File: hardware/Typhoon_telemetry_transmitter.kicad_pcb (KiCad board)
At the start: 2 copper layers, 36.5 x 26 mm, 20 parts, among them J1 Conn_01x04_Pin, J3 Conn_ST_STDC14, SW1 SW_Push, U1 STM32F103C8Tx, U2 NRF24L01_Breakout, Y1 8M

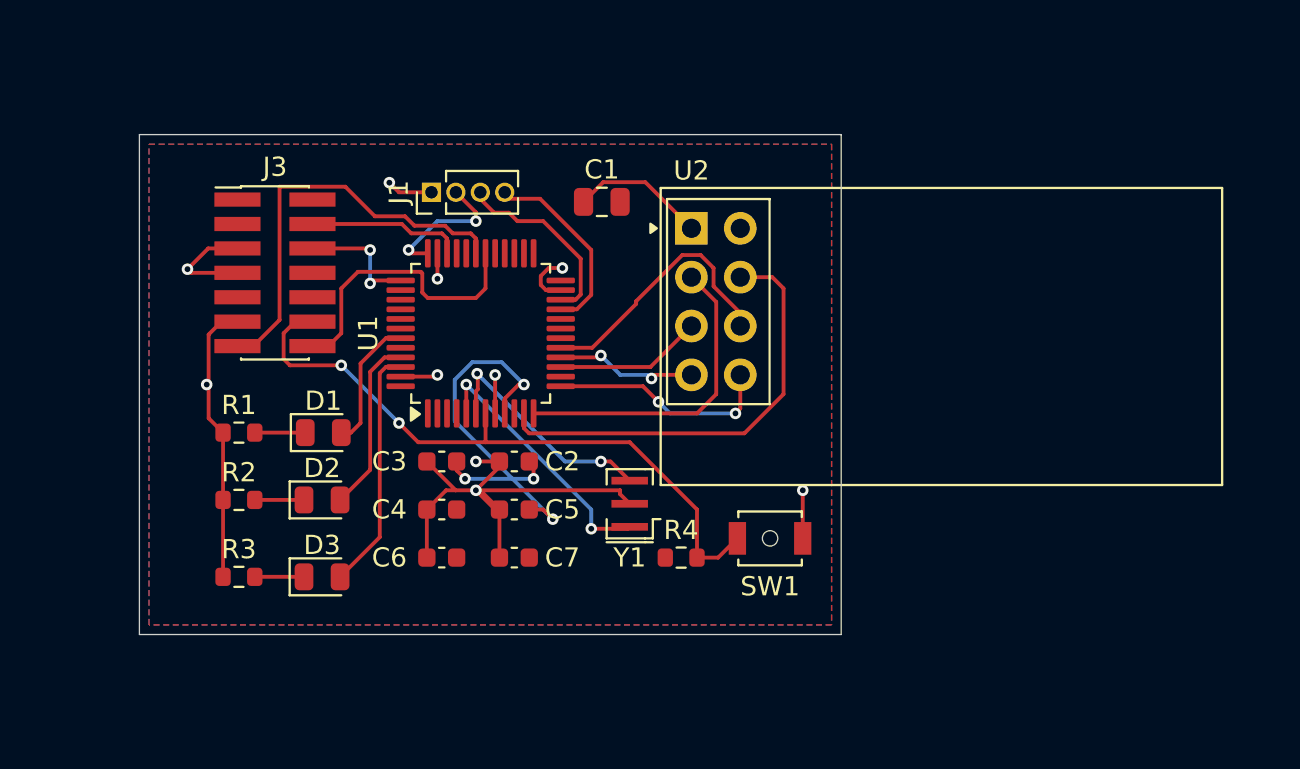
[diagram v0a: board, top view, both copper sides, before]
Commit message: Updated debugger, pull down resistors
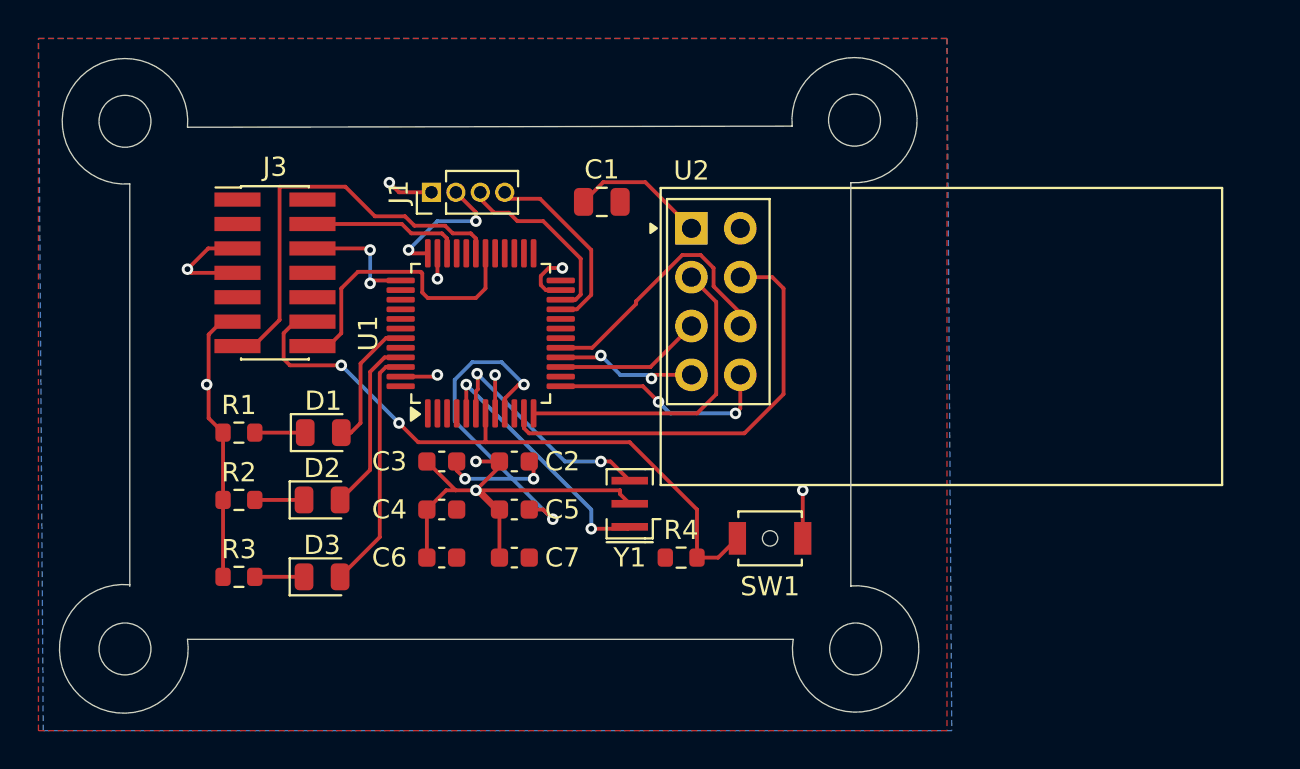
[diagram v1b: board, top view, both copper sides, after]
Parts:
- added H1: M2.5, MountingHole:MountingHole_2.7mm_M2.5, F.Cu at (170.8, 93.8)
- added H1: M2.5, MountingHole:MountingHole_2.7mm_M2.5, F.Cu at (132.8, 93.8)
- added H1: M2.5, MountingHole:MountingHole_2.7mm_M2.5, F.Cu at (170.7, 66.2)
- added H1: M2.5, MountingHole:MountingHole_2.7mm_M2.5, F.Cu at (132.8, 66.3)
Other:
- board size 36.5 x 26 mm -> 44.7 x 34.1 mm

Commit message: Final Update
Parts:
- added C8: 0.1u, Capacitor_SMD:C_0603_1608Metric, F.Cu at (155.0, 91.8)
- added JP1: Jumper_2_Open, Jumper:SolderJumper-2_P1.3mm_Open_RoundedPad1.0x1.5mm, F.Cu at (145.1, 92.0)
- added R4: 10k, Resistor_SMD:R_0603_1608Metric, F.Cu at (144.8, 81.0)
- added R5: 10k, Resistor_SMD:R_0603_1608Metric, F.Cu at (139.4, 92.0)
- J1: footprint Connector_PinHeader_1.27mm:PinHeader_1x04_P1.27mm_Vertical -> Connector_JST:JST_EH_B4B-EH-A_1x04_P2.50mm_Vertical
- moved J1 3.28 mm to (148.0, 66.8), turned to 0 degrees
- moved D3 2.63 mm to (145.0, 88.3)
- moved C1 2.07 mm to (159.6, 71.0)
- moved C2 2.07 mm to (155.0, 84.5)
- moved C3 2.07 mm to (151.2, 84.5)
- moved C4 2.07 mm to (151.2, 87.0)
- moved C5 2.07 mm to (155.0, 87.0)
- moved C6 2.07 mm to (151.2, 89.5)
- moved C7 2.07 mm to (155.0, 89.5)
- moved D1 2.07 mm to (145.1, 83.0)
- moved R4 2.07 mm to (163.7, 89.5)
- moved SW1 2.07 mm to (168.3, 88.5)
- moved U2 2.07 mm to (164.2, 72.4)
- moved Y1 2.07 mm to (161.0, 86.7)
- moved U1 2.07 mm to (153.2, 77.9)
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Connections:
- net /Programming_RX renamed /STLINK_{RX}
- net /Programming_TX renamed /STLINK_{TX}
- net /codeclk renamed /SWCLK
- net /codeio renamed /SWDIO
- J3 pad 12: /Reset -> Net-(J3-~{RST})
- J3 pad 8: unconnected-(J3-JTDO/SWO-Pad8) -> /SWO
- U1 pad 39: unconnected-(U1-PB3-Pad39) -> /SWO
- U1 pad 44: unconnected-(U1-BOOT0-Pad44) -> Net-(U1-BOOT0)
- U1 pad 7: /Reset -> unconnected-(U1-NRST-Pad7)
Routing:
- net /Reset: track 34.3 -> 2.51 mm, vias 2 -> 0
- net Net-(J3-~{RST}): track 0.00 -> 21.9 mm
- net GND: track 65.5 -> 49.4 mm, vias 10 -> 14
- net Net-(U1-BOOT0): track 0.00 -> 14.5 mm, vias 0 -> 2
- net /SWO: track 0.00 -> 5.50 mm, vias 0 -> 2
- net /RX: track 9.52 -> 12.5 mm
- net Net-(D3-A): track 12.7 -> 10.4 mm
- net /TX: track 10.1 -> 12.3 mm
- net Net-(D3-K): track 2.56 -> 3.81 mm
- net Net-(D2-K): track 2.56 -> 3.81 mm
- net Net-(D1-K): track 2.62 -> 3.80 mm
- net +3.3V: track 30.1 -> 31.2 mm, vias 6 -> 5
- net Net-(D2-A): track 9.21 -> 8.21 mm
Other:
- board size 44.7 x 34.1 mm -> 45 x 34.5 mm

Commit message: Final Final Updates
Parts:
- moved C1 0.81 mm to (158.8, 70.8)
- moved C2 0.81 mm to (154.2, 84.2)
- moved C3 0.81 mm to (150.5, 84.2)
- moved C4 0.81 mm to (150.5, 86.8)
- moved C5 0.81 mm to (154.2, 86.8)
- moved C6 0.81 mm to (150.5, 89.2)
- moved C7 0.81 mm to (154.2, 89.2)
- moved C8 0.81 mm to (154.2, 91.5)
- moved D1 0.81 mm to (144.3, 82.8)
- moved D2 0.81 mm to (144.2, 85.2)
- moved D3 0.81 mm to (144.2, 88.0)
- moved J1 0.81 mm to (147.2, 66.5)
- moved JP1 0.81 mm to (144.3, 91.8)
- moved R1 0.81 mm to (138.8, 82.8)
- moved R2 0.81 mm to (138.7, 85.2)
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
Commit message: Final Update and Production done
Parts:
- moved SW1 7.28 mm to (160.6, 90.3)
- moved H1 4.44 mm to (170.7, 89.3)
- moved H1 4.44 mm to (132.8, 89.3)
- moved R4 1.53 mm to (163.6, 87.9)
- moved R5 1.32 mm to (138.5, 90.4)
- moved JP1 1.32 mm to (144.1, 90.4)
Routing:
- net GND: track 49.4 -> 41.1 mm, vias 14 -> 15
- net /Reset: track 2.51 -> 6.53 mm
- net Net-(J3-~{RST}): track 21.9 -> 19.6 mm, vias 0 -> 2
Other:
- board size 45 x 34.5 mm -> 45 x 30 mm
- board text added: "RESET"
- board text added: "TYPHOON TELEMETRY J. LO"
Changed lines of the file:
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@@
 		(tags "SMD SMT ceramic resonator filter")
 		(property "Reference" "Y1"
-			(at -2.8 0 0)
+			(at 2.6554 0.1002 0)
 			(layer "F.SilkS")
 			(effects
@@
 	(footprint "MountingHole:MountingHole_2.7mm_M2.5"
 		(layer "F.Cu")
-		(at 170.75 93.75 90)
+		(at 170.691429 89.3064 90)
 		(descr "Mounting Hole 2.7mm, no annular, M2.5")
 		(tags "mounting hole 2.7mm no annular m2.5")
@@
 	(footprint "Resistor_SMD:R_0603_1608Metric"
 		(layer "F.Cu")
-		(at 162.925 89.25)
+		(at 163.5506 87.8586)
 		(descr "Resistor SMD 0603 (1608 Metric), square (rectangular) end terminal, IPC_7351 nominal, (Body size source: IPC-SM-782 page 72, https://www.pcb-3d.com/wordpress/wp-content/uploads/ipc-sm-782a_amendment_1_and_2.pdf), generated with kicad-footprint-generator")
 		(tags "resistor")
@@
 		(tags "capacitor")
 		(property "Reference" "C8"
-			(at -2.5 0 360)
+			(at -2.5 0 0)
 			(layer "F.SilkS")
 			(effects
@@
 		)
 		(property "Value" "0.1u"
-			(at 0 1.43 360)
+			(at 0 1.43 0)
 			(layer "F.Fab")
 			(effects
@@
 		)
 		(fp_text user "${REFERENCE}"
-			(at 0 0 360)
+			(at 0 0 0)
 			(layer "F.Fab")
 			(effects
@@
 	(footprint "MountingHole:MountingHole_2.7mm_M2.5"
 		(layer "F.Cu")
-		(at 132.75 93.75)
+		(at 132.75 89.3064)
 		(descr "Mounting Hole 2.7mm, no annular, M2.5")
 		(tags "mounting hole 2.7mm no annular m2.5")
@@
 	(footprint "Jumper:SolderJumper-2_P1.3mm_Open_RoundedPad1.0x1.5mm"
 		(layer "F.Cu")
-		(at 144.35 91.75 180)
+		(at 144.145 90.4494 180)
 		(descr "SMD Solder Jumper, 1x1.5mm, rounded Pads, 0.3mm gap, open")
 		(tags "solder jumper open")
 		(property "Reference" "JP1"
-			(at 0 -1.8 360)
+			(at 0 -1.8 0)
 			(layer "F.SilkS")
 			(effects
@@
 		)
 		(property "Value" "Jumper_2_Open"
-			(at 0 1.9 360)
+			(at 0 1.9 0)
 			(layer "F.Fab")
 			(effects
@@
 		(tags "resistor")
 		(property "Reference" "R4"
-			(at -2.75 0 360)
+			(at -2.75 0 0)
 			(layer "F.SilkS")
 			(effects
@@
 		)
 		(property "Value" "10k"
-			(at 0 1.43 360)
+			(at 0 1.43 0)
 			(layer "F.Fab")
 			(effects
@@
 		)
 		(fp_text user "${REFERENCE}"
-			(at 0 0 360)
+			(at 0 0 0)
 			(layer "F.Fab")
 			(effects
@@
 	(footprint "Button_Switch_SMD:SW_SPST_B3U-1000P-B"
 		(layer "F.Cu")
-		(at 167.55 88.25 180)
+		(at 160.5788 90.3478 180)
 		(descr "Ultra-small-sized Tactile Switch with High Contact Reliability, Top-actuated Model, without Ground Terminal, with Boss")
 		(tags "Tactile Switch")
 		(property "Reference" "SW1"
-			(at 0 -2.5 180)
+			(at -4.1402 0.635 180)
 			(layer "F.SilkS")
 			(effects
@@
 			(at 0 2.5 180)
 			(layer "F.Fab")
+			(hide yes)
 			(effects
 				(font
@@
 		(tags "connector JST EH vertical")
 		(property "Reference" "J1"
-			(at 3.75 3.5 360)
+			(at 3.75 3.5 0)
 			(layer "F.SilkS")
 			(effects
@@
 		)
 		(property "Value" "Conn_01x04_Pin"
-			(at 3.75 3.4 360)
+			(at 3.75 3.4 0)
 			(layer "F.Fab")
 			(effects
@@
 		)
 		(fp_text user "${REFERENCE}"
-			(at 3.75 1.5 360)
+			(at 3.75 1.5 0)
 			(layer "F.Fab")
 			(effects
@@
 		(tags "resistor")
 		(property "Reference" "R3"
-			(at -3.175 0 0)
+			(at -2.8104 -1.1828 0)
 			(layer "F.SilkS")
 			(effects
@@
 	(footprint "Resistor_SMD:R_0603_1608Metric"
 		(layer "F.Cu")
-		(at 138.675 91.75)
+		(at 138.47 90.4494)
 		(descr "Resistor SMD 0603 (1608 Metric), square (rectangular) end terminal, IPC_7351 nominal, (Body size source: IPC-SM-782 page 72, https://www.pcb-3d.com/wordpress/wp-content/uploads/ipc-sm-782a_amendment_1_and_2.pdf), generated with kicad-footprint-generator")
 		(tags "resistor")
 		(property "Reference" "R5"
-			(at 0 -1.43 0)
+			(at -2.5292 1.27 0)
 			(layer "F.SilkS")
 			(effects
@@
 	)
 	(gr_arc
-		(start 174.25 93.75)
-		(mid 173.224874 96.224874)
-		(end 170.75 97.25)
+		(start 174.2404 89.2862)
+		(mid 173.215274 91.761074)
+		(end 170.7404 92.7862)
 		(stroke
 			(width 0.05)
@@
 	)
 	(gr_line
-		(start 132.75 97.25)
-		(end 170.75 97.25)
+		(start 132.7404 92.7862)
+		(end 170.7404 92.7862)
 		(stroke
 			(width 0.05)
@@
 	)
 	(gr_line
-		(start 174.25 93.75)
+		(start 174.2404 89.2862)
 		(end 174.25 66.25)
 		(stroke
@@
 	)
 	(gr_arc
-		(start 132.75 97.25)
-		(mid 130.275126 96.224874)
-		(end 129.25 93.75)
+		(start 132.7404 92.7862)
+		(mid 130.265526 91.761074)
+		(end 129.2404 89.2862)
 		(stroke
 			(width 0.05)
@@
 	(gr_line
 		(start 129.25 66)
-		(end 129.25 93.75)
+		(end 129.2352 89.281)
 		(stroke
 			(width 0.05)
@@
 	)
 	(gr_text "Typhoon Telemetry Transmitter\nDesigned By: Justin Lo"
-		(at 166.5 95.25 0)
+		(at 166.2684 91.9734 0)
 		(layer "B.SilkS")
 		(effects
@@
 		)
 	)
+	(gr_text "TYPHOON TELEMETRY\nJ. LO"
+		(at 130.7592 69.85 -90)
+		(layer "F.SilkS" knockout)
+		(effects
+			(font
+				(size 1 1)
+				(thickness 0.2)
+				(bold yes)
+			)
+			(justify left bottom)
+		)
+	)
+	(gr_text "RESET\n"
+		(at 163.1696 91.9226 0)
+		(layer "F.SilkS")
+		(effects
+			(font
+				(size 1 1)
+				(thickness 0.1)
+			)
+			(justify left bottom)
+		)
+	)
 	(segment
 		(start 151.25 84.715687)
@@
 	)
 	(segment
-		(start 169.25 88.25)
-		(end 169.25 85.75)
-		(width 0.2)
-		(layer "F.Cu")
-		(net 2)
-	)
-	(segment
 		(start 139.85 73.17)
 		(end 138.33 73.17)
@@
 	)
 	(segment
-		(start 145 91.75)
-		(end 147.5 89.25)
-		(width 0.2)
-		(layer "F.Cu")
-		(net 2)
-	)
-	(segment
 		(start 149.7 86.75)
 		(end 150.7 85.75)
@@
 	)
 	(segment
-		(start 147.5 89.25)
-		(end 149.7 89.25)
-		(width 0.2)
-		(layer "F.Cu")
-		(net 2)
-	)
-	(segment
 		(start 159.75 85.95)
 		(end 160.25 86.45)
@@
 	)
 	(via
+		(at 144.795 90.4494)
+		(size 0.6)
+		(drill 0.3)
+		(layers "F.Cu" "B.Cu")
+		(net 2)
+	)
+	(via
+		(at 162.3822 90.5256)
+		(size 0.6)
+		(drill 0.3)
+		(layers "F.Cu" "B.Cu")
+		(net 2)
+	)
+	(via
 		(at 157.75 70.75)
 		(size 0.6)
@@
 	)
 	(via
-		(at 169.25 85.75)
-		(size 0.6)
-		(drill 0.3)
-		(layers "F.Cu" "B.Cu")
-		(net 2)
-	)
-	(via
 		(at 139.5 76.83)
 		(size 0.6)
@@
 	)
 	(segment
-		(start 164.85 89.25)
-		(end 165.85 88.25)
+		(start 158.8788 90.3478)
+		(end 160.593 88.6336)
+		(width 0.2)
+		(layer "F.Cu")
+		(net 11)
+	)
+	(segment
+		(start 160.593 88.6336)
+		(end 163.6006 88.6336)
 		(width 0.2)
 		(layer "F.Cu")
@@
 	)
 	(segment
-		(start 163.75 89.25)
-		(end 164.85 89.25)
+		(start 163.6006 88.6336)
+		(end 164.3756 87.8586)
 		(width 0.2)
 		(layer "F.Cu")
@@
 	)
 	(segment
-		(start 139.5 91.75)
-		(end 143.7 91.75)
+		(start 142.0114 89.5604)
+		(end 142.0114 90.3732)
 		(width 0.2)
 		(layer "F.Cu")
@@
 	)
 	(segment
-		(start 141 79.25)
-		(end 138.75 81.5)
+		(start 141.8082 77.5918)
+		(end 141.8082 79.4766)
 		(width 0.2)
 		(layer "F.Cu")
@@
 	)
 	(segment
-		(start 141 78.33)
-		(end 141 79.25)
+		(start 143.4 76.83)
+		(end 142.57 76.83)
 		(width 0.2)
 		(layer "F.Cu")
@@
 	)
 	(segment
-		(start 142.5 76.83)
-		(end 141 78.33)
+		(start 142.57 76.83)
+		(end 141.8082 77.5918)
 		(width 0.2)
 		(layer "F.Cu")
@@
 	)
 	(segment
-		(start 138.75 91)
-		(end 139.5 91.75)
+		(start 139.295 90.4494)
+		(end 141.9352 90.4494)
 		(width 0.2)
 		(layer "F.Cu")
@@
 	)
 	(segment
-		(start 138.75 81.5)
-		(end 138.75 91)
+		(start 141.9352 90.4494)
+		(end 143.495 90.4494)
 		(width 0.2)
 		(layer "F.Cu")
@@
 	)
 	(segment
-		(start 143.4 76.83)
-		(end 142.5 76.83)
+		(start 142.0114 90.3732)
+		(end 141.9352 90.4494)
 		(width 0.2)
 		(layer "F.Cu")
 		(net 51)
 	)
+	(via
+		(at 141.8082 79.4766)
+		(size 0.6)
+		(drill 0.3)
+		(layers "F.Cu" "B.Cu")
+		(net 51)
+	)
+	(via
+		(at 142.0114 89.5604)
+		(size 0.6)
+		(drill 0.3)
+		(layers "F.Cu" "B.Cu")
+		(net 51)
+	)
+	(segment
+		(start 141.8082 79.4766)
+		(end 141.15 80.1348)
+		(width 0.2)
+		(layer "B.Cu")
+		(net 51)
+	)
+	(segment
+		(start 141.15 80.1348)
+		(end 141.15 88.699)
+		(width 0.2)
+		(layer "B.Cu")
+		(net 51)
+	)
+	(segment
+		(start 141.15 88.699)
+		(end 142.0114 89.5604)
+		(width 0.2)
+		(layer "B.Cu")
+		(net 51)
+	)
